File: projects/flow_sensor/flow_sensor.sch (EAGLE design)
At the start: 59 parts, among them IC1 TPS61201, IC5 REG1118

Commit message: Adjusted AD8222 schematic part
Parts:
- removed D1, D2, D3, D4: 1N4004, diode:1N4004
- added U$3: BAS4002A, my_library:BAS4002A
- added U$4: AD8222, my_library:AD8222
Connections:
- removed net N$31: COIL.2, D1.A, D2.C
- removed net N$32: COIL.1, D3.A, D4.C
- new net N$1: COIL.2, U$3.~
- new net N$30: C30.1, IC5.VIN, U$3.+
- net 3.3V: now also U$3.-; no longer D2.A, D4.A
- net N$27: now also COIL.1, U$3.~'; no longer C30.1, D1.C, D3.C, IC5.VIN
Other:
- moved on the sheet: C28, C29, R10, R11, R8, R9

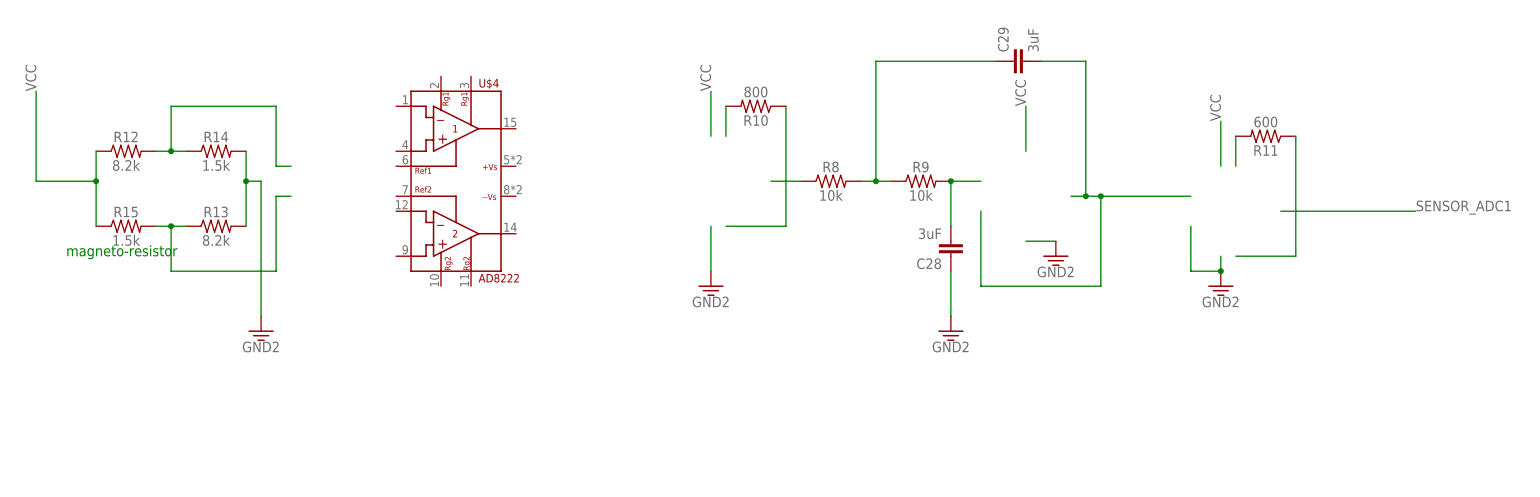
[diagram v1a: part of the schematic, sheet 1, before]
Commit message: AD8222 modified in library and connected in schematic
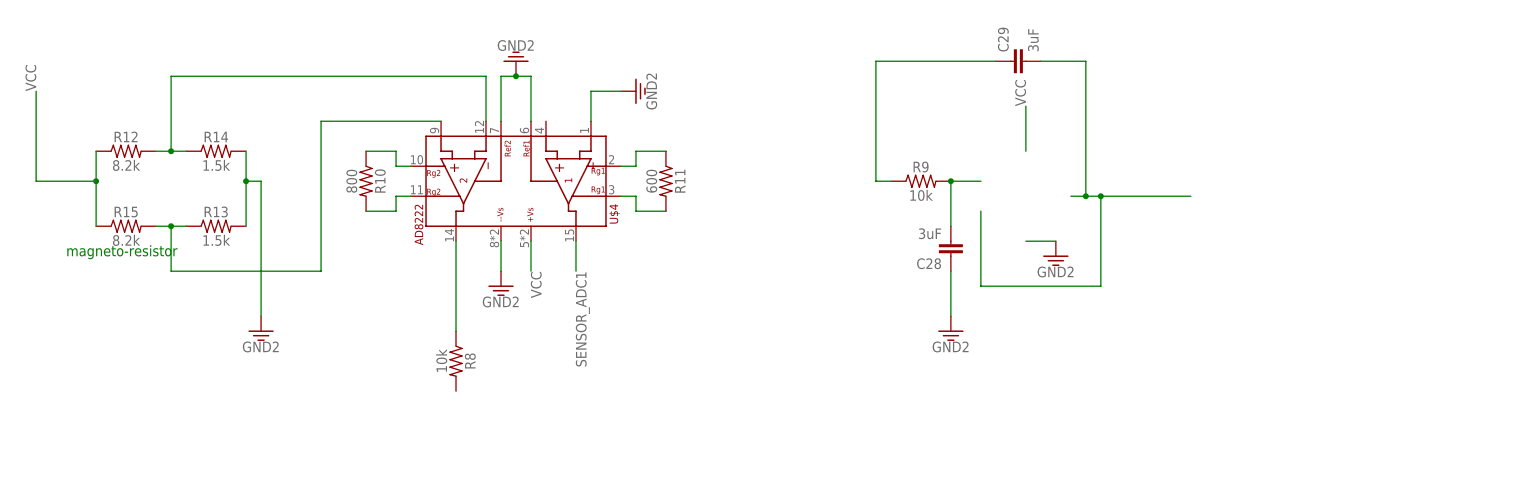
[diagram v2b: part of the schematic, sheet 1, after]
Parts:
- R13: value 8.2k -> 1.5k
- R15: value 1.5k -> 8.2k
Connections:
- net 3.3V: now also U$4.-IN1, U$4.REF1, U$4.REF2
- net N$19: no longer R8.2
- net N$23: now also R10.1, U$4.RG2; no longer R10.2
- net N$24: now also R10.2, U$4.RG2'; no longer R10.1
- net N$25: now also R11.1, U$4.RG1; no longer R11.2
- net N$26: now also R11.2, U$4.RG1'; no longer R11.1
- net N$28: now also U$4.-IN2
- net N$29: now also U$4.+IN2
- net VCC: now also U$4.+VS
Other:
- moved on the sheet: R10, R11, R8

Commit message: Added LM8209 to library, finished sensor schematic
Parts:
- added C31, C32, C33, C34, C35, C36: 3uF, SparkFun-Capacitors:4.7UF0603
- added R16, R17, R18, R19, R20, R21: 10k, SparkFun-Resistors:10KOHM-0603-1/10W-1%
- added R22, R28, R34: 800, SparkFun-Resistors:787OHM-0603-1/10W-1%
- added R23, R29, R35: 600, SparkFun-Resistors:680OHM-0603-1/10W-5%
- added R24, R30, R36: 8.2k, SparkFun-Resistors:8.2KOHM-0603-1/10W-5%
- added R25, R31, R37: 1.5k, SparkFun-Resistors:8.2KOHM-0603-1/10W-5%
- added R26, R32, R38: 1.5k, SparkFun-Resistors:1.5KOHM-0603-1/10W-1%
- added R27, R33, R39: 8.2k, SparkFun-Resistors:1.5KOHM-0603-1/10W-1%
- added U$5: LM2902, my_library:LM2902
- added U$6, U$7, U$8: AD8222, my_library:AD8222
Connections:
- new net N$31: C34.1, R16.2, R17.1
- new net N$32: R30.2, R32.1, U$7.-IN2
- new net N$33: R31.1, R33.2, U$7.+IN2
- new net N$34: R28.1, U$7.RG2
- new net N$35: C29.1, R8.2, R9.1
- new net N$36: C31.1, R17.2
- new net N$37: R37.1, R39.2, U$8.+IN2
- new net N$38: C35.1, R18.2, R19.1
- new net N$39: C32.1, R19.2
- new net N$40: R34.1, U$8.RG2
- new net N$41: C36.1, R20.2, R21.1
- new net N$42: C33.1, R21.2
- new net N$43: R24.2, R26.1, U$6.-IN2
- new net N$44: R25.1, R27.2, U$6.+IN2
- new net N$45: R28.2, U$7.RG2'
- new net N$46: R29.1, U$7.RG1
- new net N$47: R22.1, U$6.RG2
- new net N$48: R22.2, U$6.RG2'
- new net N$49: R23.1, U$6.RG1
- new net N$50: R23.2, U$6.RG1'
- new net N$51: R29.2, U$7.RG1'
- new net N$52: R34.2, U$8.RG2'
- new net N$53: R35.1, U$8.RG1
- new net N$54: R35.2, U$8.RG1'
- new net OPAMP1_OUT: C29.2, U$4.+IN1, U$5.IN1-, U$5.OUT1
- new net OPAMP2_OUT: C34.2, U$5.IN2-, U$5.OUT2, U$6.+IN1
- new net OPAMP3_IN: R18.1, U$7.OUT2
- new net OPAMP3_OUT: C35.2, U$5.IN3-, U$5.OUT3, U$7.+IN1
- new net OPAMP4_IN: R20.1, U$8.OUT2
- new net OPAMP4_OUT: C36.2, U$5.IN4-, U$5.OUT4, U$8.+IN1
- new net SENSOR_ADC1: U$4.OUT1
- new net SENSOR_ADC2: U$6.OUT1
- new net SENSOR_ADC3: U$7.OUT1
- new net SENSOR_ADC4: U$8.OUT1
- net 3.3V: now also C28.2, C31.2, C32.2, C33.2, R25.2, R26.2, R31.2, R32.2, R37.2, R38.2, U$6.-IN1, U$6.REF1, U$6.REF2, U$7.-IN1, U$7.REF1, U$7.REF2, U$8.-IN1, U$8.REF1, U$8.REF2; no longer C28.1
- net GND: now also U$4.-VS, U$5.VCC-, U$6.-VS, U$7.-VS, U$8.-VS
- net N$18: now also U$4.OUT2
- net N$19: now also C28.1, R9.2, U$5.IN1+; no longer C29.1, R9.1
- net N$21: now also R16.1, U$6.OUT2; no longer C28.2, R9.2
- net N$22: now also R36.2, R38.1, U$8.-IN2; no longer C29.2
- net VCC: now also R24.1, R27.1, R30.1, R33.1, R36.1, R39.1, U$5.VCC+, U$6.+VS, U$7.+VS, U$8.+VS
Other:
- moved on the sheet: C28, C29, R10, R11, R12, R13, R14, R15, R8, R9, U$4

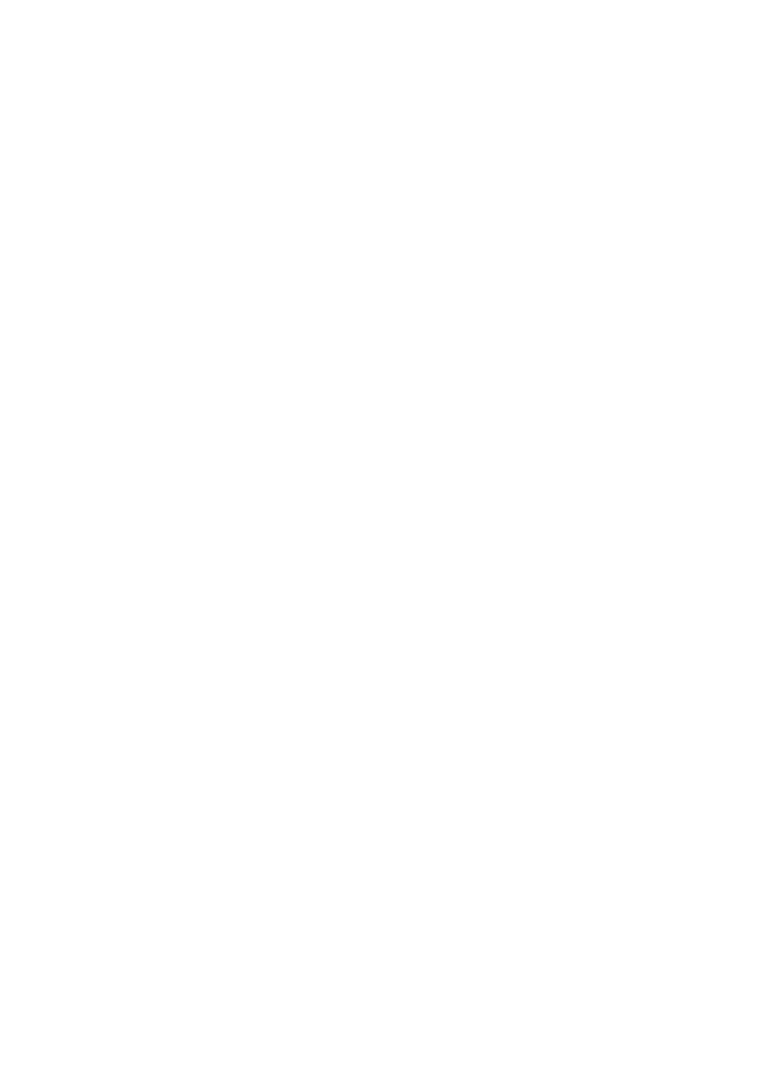
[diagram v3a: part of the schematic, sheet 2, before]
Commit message: Completed MSP430FR5994 part in library
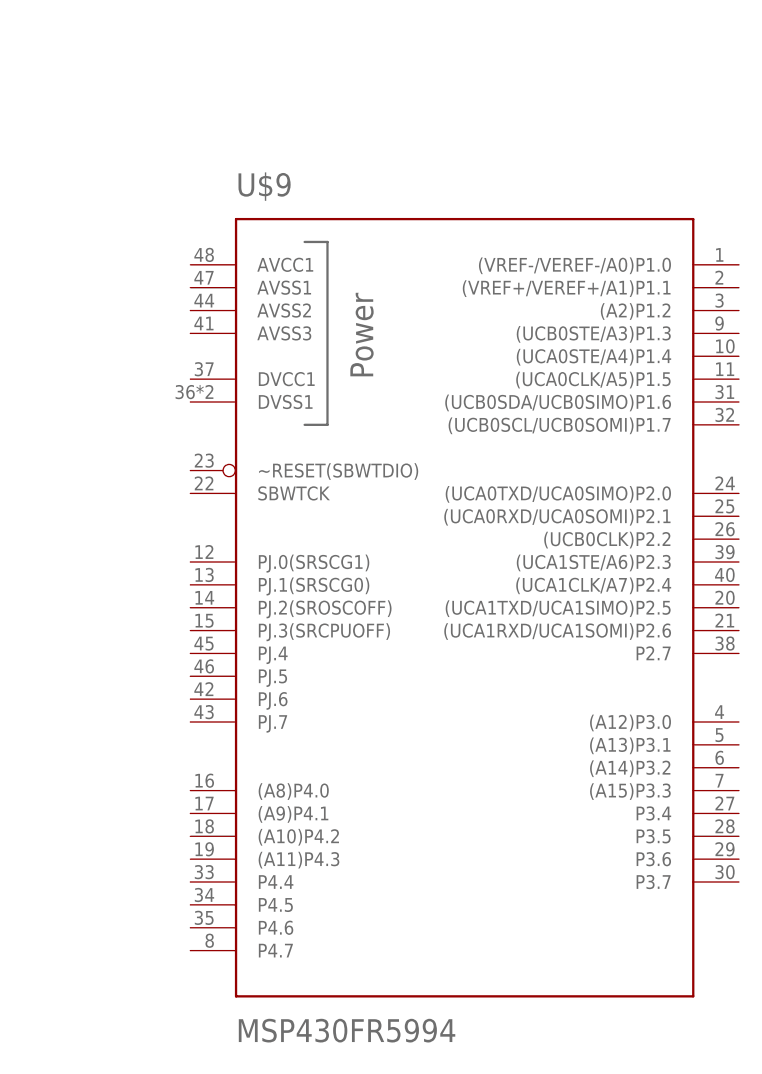
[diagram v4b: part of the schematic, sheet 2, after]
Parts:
- added U$9: MSP430FR5994, my_library:MSP430FR5994
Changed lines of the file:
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@@
 <part name="GND41" library="SparkFun-PowerSymbols" deviceset="GND2" device=""/>
 <part name="GND42" library="SparkFun-PowerSymbols" deviceset="GND2" device=""/>
+<part name="FRAME4" library="SparkFun-Aesthetics" deviceset="FRAME-A4L" device="">
+<attribute name="CNAME" value="Microcontroller"/>
+<attribute name="CREVISION" value=""/>
+<attribute name="DESIGNER" value="A Osborn, M Silver, N Yokley"/>
+</part>
+<part name="U$9" library="my_library" deviceset="MSP430FR5994" device=""/>
 </parts>
 <sheets>
@@
 <instance part="GND14" gate="G$1" x="22.86" y="15.24"/>
 <instance part="GND15" gate="G$1" x="33.02" y="15.24"/>
+<instance part="FRAME4" gate="G$1" x="162.56" y="-91.44">
+<attribute name="DESIGNER" x="162.56" y="-91.44" size="1.778" layer="96" display="off"/>
+<attribute name="CNAME" x="162.56" y="-91.44" size="1.6764" layer="96" display="off"/>
+<attribute name="CREVISION" x="162.56" y="-91.44" size="1.6764" layer="96" display="off"/>
+</instance>
+<instance part="U$9" gate="G$1" x="287.02" y="2.54"/>
 </instances>
 <busses>

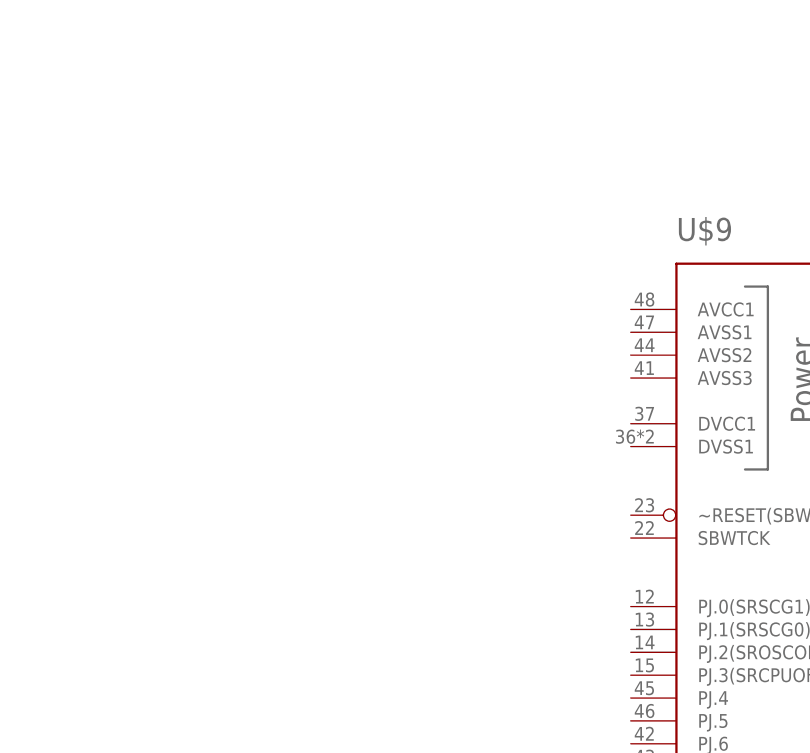
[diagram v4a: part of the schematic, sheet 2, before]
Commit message: fixed BAS4002A pinout, added decoupling capacitors to uC
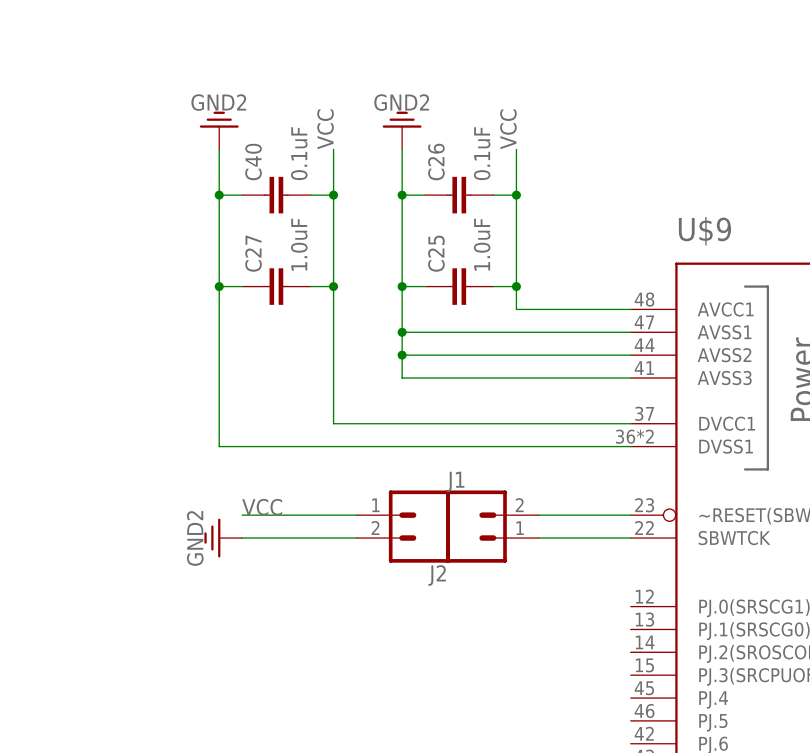
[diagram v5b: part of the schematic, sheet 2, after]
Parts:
- added C37, C40: 0.1uF, SparkFun-Capacitors:0.1UF-0603-25V-(+80/-20%)
- added C38, C39: 10uF, SparkFun-Capacitors:10UF-0603-6.3V-20%
- added J1, J2: (no value), SparkFun-Connectors:CONN_02
- C1, C2: device rcl:C-USC0805 -> SparkFun-Capacitors:4.7UF0603
- C23: device SparkFun-Capacitors:100PF-0402-50V-5% -> SparkFun-Capacitors:100PF-0603-50V-5%
- C24: device SparkFun-Capacitors:100PF-0402-50V-5% -> SparkFun-Capacitors:27PF-0603-50V-5%
- C25, C27: value 10uF -> 1.0uF; device SparkFun-Capacitors:10UF-0805-10V-10% -> SparkFun-Capacitors:1.0UF-0603-16V-10%
- C26: device SparkFun-Capacitors:0.1UF-0402-16V-10% -> SparkFun-Capacitors:0.1UF-0603-25V-(+80/-20%)
- C30: device rcl:C-USC0805 -> SparkFun-Capacitors:10UF-0603-6.3V-20%
- L1, L2: device SparkFun-Coils:INDUCTOR-0402-3.9NH -> SparkFun-Coils:INDUCTOR-0603-33NH
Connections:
- removed net 3.3V: C28.2, C30.2, C31.2, C32.2, C33.2, IC5.GND, R13.2, R14.2, R25.2, R26.2, R31.2, R32.2, R37.2, R38.2, U$3.-, U$4.-IN1, U$4.REF1, U$4.REF2, U$6.-IN1, U$6.REF1, U$6.REF2, U$7.-IN1, U$7.REF1, U$7.REF2, U$8.-IN1, U$8.REF1, U$8.REF2
- new net N$55: J1.2, U$9.~RESET(SBWTDIO)
- new net N$56: J1.1, U$9.SBWTCK
- net GND: now also C25.1, C27.1, C28.2, C30.2, C31.2, C32.2, C33.2, C37.2, C38.2, C39.2, C40.1, IC5.GND, J2.2, R13.2, R14.2, R25.2, R26.2, R31.2, R32.2, R37.2, R38.2, U$3.-, U$4.-IN1, U$4.REF1, U$4.REF2, U$6.-IN1, U$6.REF1, U$6.REF2, U$7.-IN1, U$7.REF1, U$7.REF2, U$8.-IN1, U$8.REF1, U$8.REF2, U$9.AVSS1, U$9.AVSS2, U$9.AVSS3, U$9.DVSS1; no longer C25.2, C27.2
- net N$3: now also C37.1; no longer C26.2
- net VCC: now also C25.2, C26.2, C27.2, C38.1, C39.1, C40.2, J2.1, U$9.AVCC1, U$9.DVCC1; no longer C25.1, C27.1
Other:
- moved on the sheet: C2, C30
